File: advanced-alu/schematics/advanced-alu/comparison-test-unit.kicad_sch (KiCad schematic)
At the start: 6 parts

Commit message: updated ALU design
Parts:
- added U?: 74LS245, symbol 74xx:74LS245
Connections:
- net CMPi: now also U?.19 (CE); no longer U?.19 (CE)
- net GND: now also U?.19 (CE), U?.10 (GND)
- net HI_TMP_0: now also U?.2 (A0); no longer U?.2 (P0)
- net HI_TMP_1: now also U?.3 (A1); no longer U?.4 (P1)
- net HI_TMP_2: now also U?.4 (A2); no longer U?.6 (P2)
- net HI_TMP_3: now also U?.5 (A3); no longer U?.8 (P3)
- net HI_TMP_4: now also U?.6 (A4); no longer U?.11 (P4)
- net HI_TMP_5: now also U?.7 (A5); no longer U?.13 (P5)
- net HI_TMP_6: now also U?.8 (A6); no longer U?.15 (P6)
- net HI_TMP_7: now also U?.9 (A7); no longer U?.17 (P7)
- net VCC: now also U?.1 (A->B), U?.20 (VCC)
- net at U?.12 (Q4), U?.14 (B4), U?.15 (I4): no longer RN?.5 (R4)
- net at U?.13 (B5), U?.14 (I5), U?.14 (Q5): no longer RN?.4 (R3)
- net at U?.12 (B6), U?.13 (I6), U?.16 (Q6): no longer RN?.3 (R2)
- net at U?.11 (B7), U?.12 (I7), U?.18 (Q7): no longer RN?.2 (R1)
- net at U?.18 (B0), U?.3 (Q0), U?.4 (I0): no longer RN?.9 (R8)
- net at U?.17 (B1), U?.3 (I1), U?.5 (Q1): no longer RN?.8 (R7)
- net at U?.16 (B2), U?.2 (I2), U?.7 (Q2): no longer RN?.7 (R6)
- net at U?.1 (I3), U?.15 (B3), U?.9 (Q3): no longer RN?.6 (R5)
- new net: RN?.5 (R4), U?.11 (P4), U?.14 (B4)
- new net: RN?.4 (R3), U?.13 (B5), U?.13 (P5)
- new net: RN?.3 (R2), U?.12 (B6), U?.15 (P6)
- new net: RN?.2 (R1), U?.11 (B7), U?.17 (P7)
- new net: RN?.9 (R8), U?.18 (B0), U?.2 (P0)
- new net: RN?.8 (R7), U?.17 (B1), U?.4 (P1)
- new net: RN?.7 (R6), U?.16 (B2), U?.6 (P2)
- new net: RN?.6 (R5), U?.15 (B3), U?.8 (P3)
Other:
- note added: "In CMP mode, the E(quals) flag is set when data bus and HI_TMP values are equal, and the O(verflow) flag is set when value in HI_TMP register is greater than the value on the data bus. Otherwise, E flag is set when data bus value is zero."
- note removed: "In CMP mode, the E(quals) flag is set when values are equal, and the O(verflow) flag is set when value in HI_TMP register is greater than the value on the data bus."
- moved on the sheet: RN?

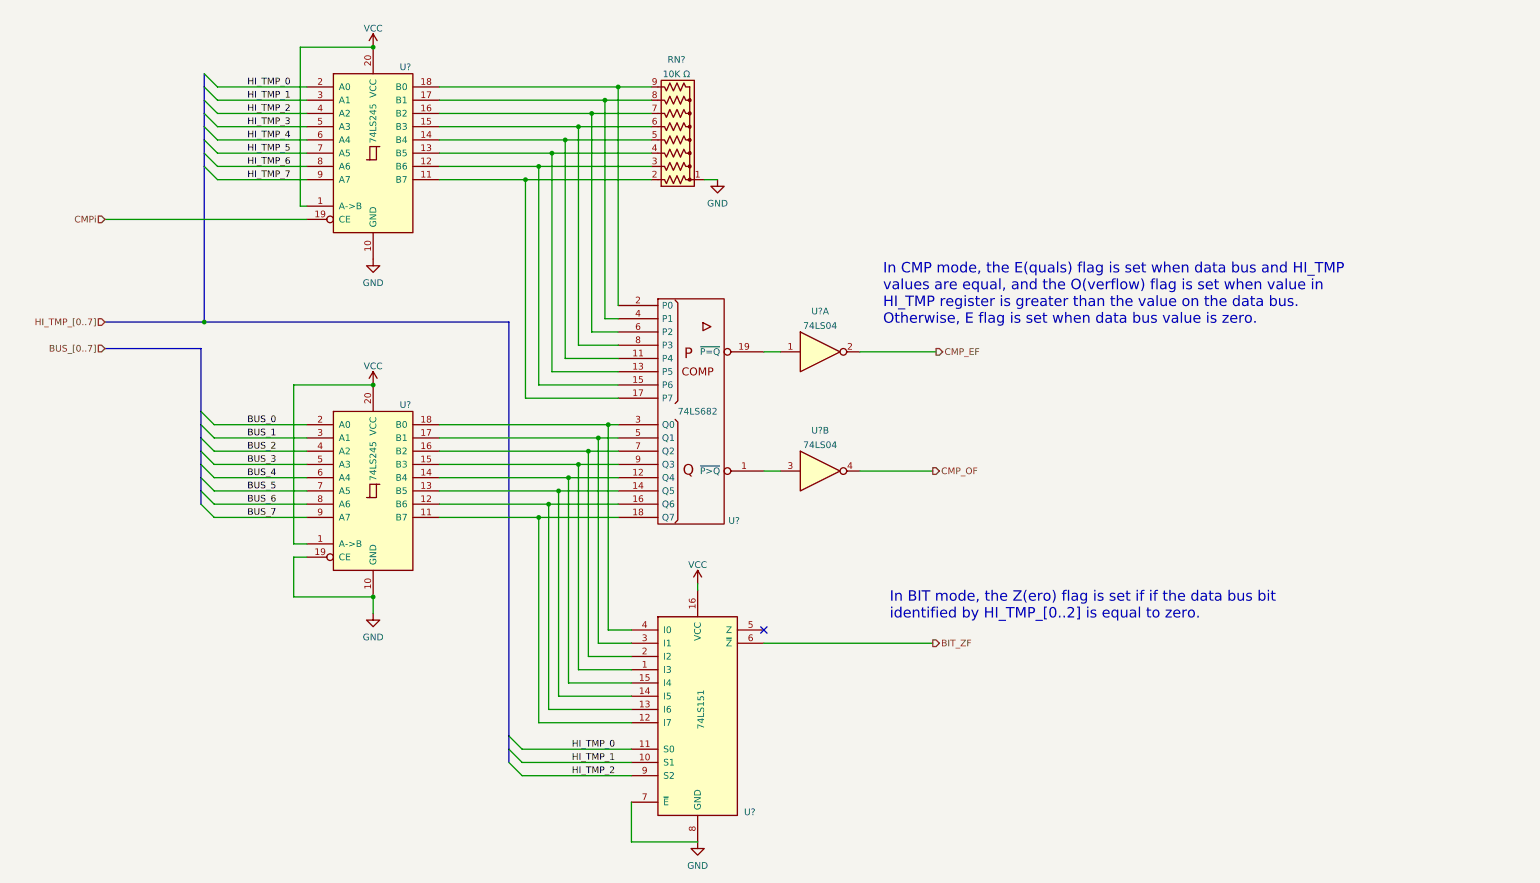
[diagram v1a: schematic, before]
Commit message: updated flags register
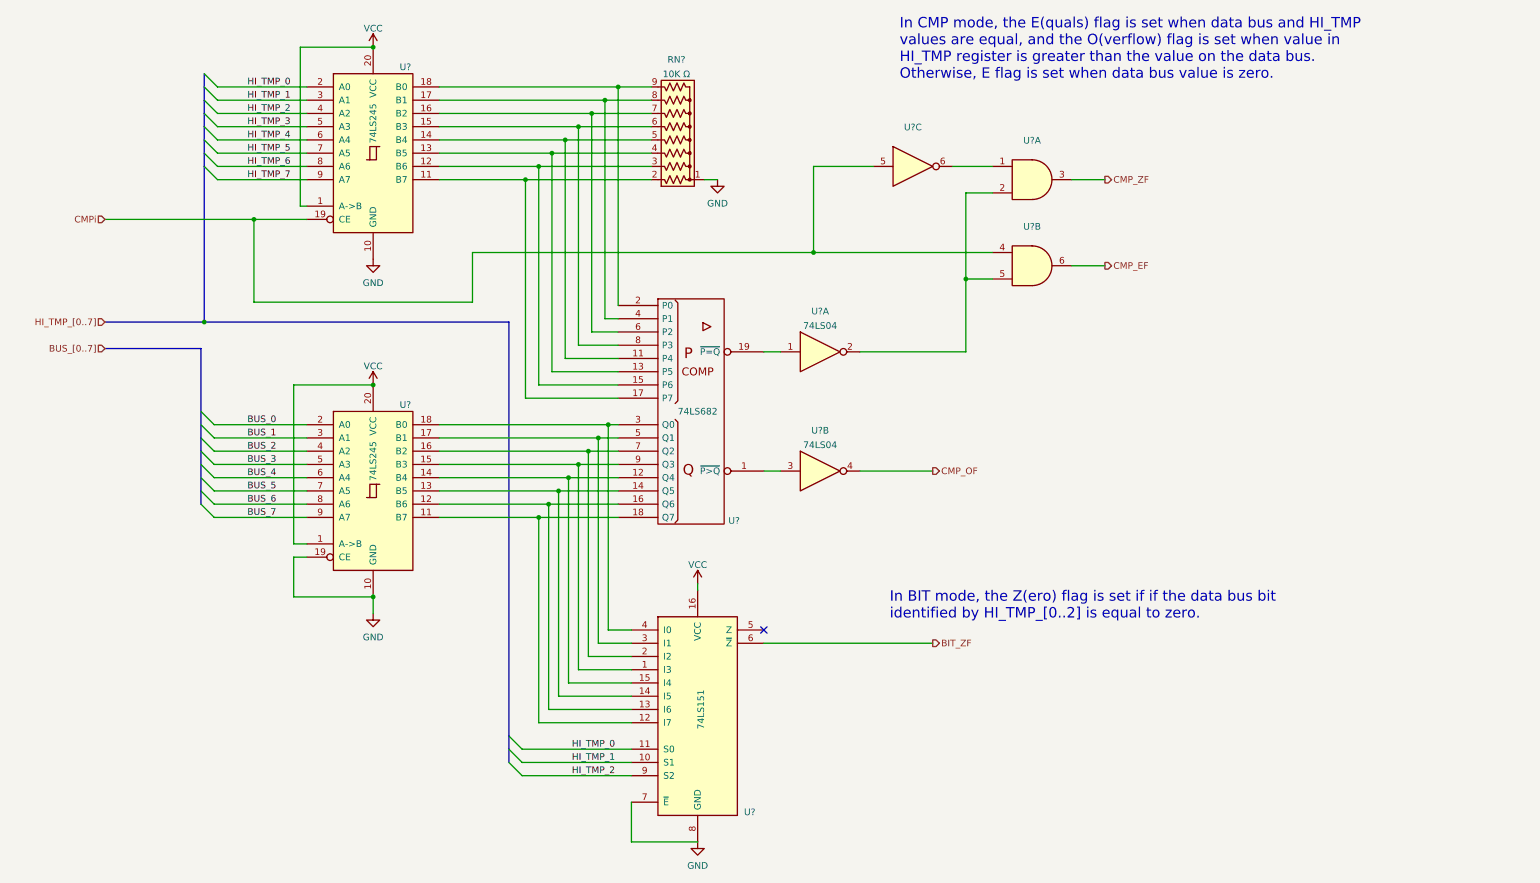
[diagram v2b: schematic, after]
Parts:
- added U? (x2): (no value), symbol 74xx:74LS08
- added U?: (no value), symbol 74xx:74LS04
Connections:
- net CMP_EF: now also U?.6; no longer U?.2
- net CMPi: now also U?.4, U?.5
- new net: U?.1, U?.6
- new net: U?.2, U?.2, U?.5
- new net CMP_ZF: U?.3
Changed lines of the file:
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@@
   (junction (at 114.3 46.99) (diameter 0) (color 0 0 0 0)
   )
+  (junction (at 59.69 57.15) (diameter 0) (color 0 0 0 0)
+  )
   (junction (at 121.92 39.37) (diameter 0) (color 0 0 0 0)
   )
@@
   (junction (at 82.55 129.54) (diameter 0) (color 0 0 0 0)
   )
+  (junction (at 196.215 68.58) (diameter 0) (color 0 0 0 0)
+  )
   (junction (at 82.55 88.9) (diameter 0) (color 0 0 0 0)
   )
@@
   )
   (junction (at 114.3 114.3) (diameter 0) (color 0 0 0 0)
+  )
+  (junction (at 167.005 63.5) (diameter 0) (color 0 0 0 0)
   )
   (junction (at 121.92 104.14) (diameter 0) (color 0 0 0 0)
@@
     (stroke (width 0) (type default) (color 0 0 0 0))
   )
+  (wire (pts (xy 59.69 57.15) (xy 69.85 57.15))
+    (stroke (width 0) (type default) (color 0 0 0 0))
+  )
   (wire (pts (xy 123.825 140.97) (xy 132.08 140.97))
     (stroke (width 0) (type default) (color 0 0 0 0))
@@
     (stroke (width 0) (type default) (color 0 0 0 0))
   )
+  (wire (pts (xy 167.005 63.5) (xy 167.005 46.99))
+    (stroke (width 0) (type default) (color 0 0 0 0))
+  )
   (wire (pts (xy 121.92 143.51) (xy 132.08 143.51))
     (stroke (width 0) (type default) (color 0 0 0 0))
@@
     (stroke (width 0) (type default) (color 0 0 0 0))
   )
+  (wire (pts (xy 101.6 63.5) (xy 167.005 63.5))
+    (stroke (width 0) (type default) (color 0 0 0 0))
+  )
+  (wire (pts (xy 193.675 46.99) (xy 201.295 46.99))
+    (stroke (width 0) (type default) (color 0 0 0 0))
+  )
   (wire (pts (xy 52.705 41.91) (xy 69.85 41.91))
     (stroke (width 0) (type default) (color 0 0 0 0))
@@
     (stroke (width 0) (type default) (color 0 0 0 0))
   )
+  (wire (pts (xy 59.69 57.15) (xy 59.69 73.025))
+    (stroke (width 0) (type default) (color 0 0 0 0))
+  )
   (wire (pts (xy 82.55 129.54) (xy 82.55 132.715))
     (stroke (width 0) (type default) (color 0 0 0 0))
@@
     (stroke (width 0) (type default) (color 0 0 0 0))
   )
+  (wire (pts (xy 101.6 73.025) (xy 101.6 63.5))
+    (stroke (width 0) (type default) (color 0 0 0 0))
+  )
   (wire (pts (xy 144.78 127) (xy 144.78 128.27))
     (stroke (width 0) (type default) (color 0 0 0 0))
@@
     (stroke (width 0) (type default) (color 0 0 0 0))
   )
+  (wire (pts (xy 167.005 46.99) (xy 178.435 46.99))
+    (stroke (width 0) (type default) (color 0 0 0 0))
+  )
   (wire (pts (xy 95.25 114.3) (xy 114.3 114.3))
     (stroke (width 0) (type default) (color 0 0 0 0))
   )
+  (wire (pts (xy 175.895 82.55) (xy 196.215 82.55))
+    (stroke (width 0) (type default) (color 0 0 0 0))
+  )
   (bus (pts (xy 49.53 109.22) (xy 49.53 106.68))
     (stroke (width 0) (type default) (color 0 0 0 0))
   )
+  (wire (pts (xy 201.295 52.07) (xy 196.215 52.07))
+    (stroke (width 0) (type default) (color 0 0 0 0))
+  )
   (wire (pts (xy 52.705 44.45) (xy 69.85 44.45))
     (stroke (width 0) (type default) (color 0 0 0 0))
@@
     (stroke (width 0) (type default) (color 0 0 0 0))
   )
+  (wire (pts (xy 196.215 68.58) (xy 201.295 68.58))
+    (stroke (width 0) (type default) (color 0 0 0 0))
+  )
   (wire (pts (xy 123.825 101.6) (xy 129.54 101.6))
     (stroke (width 0) (type default) (color 0 0 0 0))
@@
     (stroke (width 0) (type default) (color 0 0 0 0))
   )
+  (wire (pts (xy 196.215 52.07) (xy 196.215 68.58))
+    (stroke (width 0) (type default) (color 0 0 0 0))
+  )
   (wire (pts (xy 68.58 54.61) (xy 68.58 24.13))
     (stroke (width 0) (type default) (color 0 0 0 0))
@@
     (stroke (width 0) (type default) (color 0 0 0 0))
   )
+  (wire (pts (xy 216.535 49.53) (xy 222.885 49.53))
+    (stroke (width 0) (type default) (color 0 0 0 0))
+  )
   (wire (pts (xy 52.705 39.37) (xy 69.85 39.37))
     (stroke (width 0) (type default) (color 0 0 0 0))
@@
     (stroke (width 0) (type default) (color 0 0 0 0))
   )
-  (wire (pts (xy 31.115 57.15) (xy 69.85 57.15))
+  (wire (pts (xy 31.115 57.15) (xy 59.69 57.15))
     (stroke (width 0) (type default) (color 0 0 0 0))
   )
@@
     (stroke (width 0) (type default) (color 0 0 0 0))
   )
+  (wire (pts (xy 167.005 63.5) (xy 201.295 63.5))
+    (stroke (width 0) (type default) (color 0 0 0 0))
+  )
   (wire (pts (xy 52.705 31.75) (xy 69.85 31.75))
     (stroke (width 0) (type default) (color 0 0 0 0))
   )
+  (wire (pts (xy 216.535 66.04) (xy 222.885 66.04))
+    (stroke (width 0) (type default) (color 0 0 0 0))
+  )
   (wire (pts (xy 52.07 99.06) (xy 69.85 99.06))
     (stroke (width 0) (type default) (color 0 0 0 0))
@@
     (stroke (width 0) (type default) (color 0 0 0 0))
   )
+  (wire (pts (xy 59.69 73.025) (xy 101.6 73.025))
+    (stroke (width 0) (type default) (color 0 0 0 0))
+  )
   (wire (pts (xy 121.92 81.28) (xy 129.54 81.28))
     (stroke (width 0) (type default) (color 0 0 0 0))
@@
     (stroke (width 0) (type default) (color 0 0 0 0))
   )
-  (wire (pts (xy 175.895 82.55) (xy 190.5 82.55))
+  (wire (pts (xy 196.215 68.58) (xy 196.215 82.55))
     (stroke (width 0) (type default) (color 0 0 0 0))
   )
@@
   )
   (text "In CMP mode, the E(quals) flag is set when data bus and HI_TMP\nvalues are equal, and the O(verflow) flag is set when value in\nHI_TMP register is greater than the value on the data bus.\nOtherwise, E flag is set when data bus value is zero."
-    (at 180.34 77.47 0)
+    (at 183.515 30.48 0)
     (effects (font (size 2 2)) (justify left bottom))
   )
@@
     (effects (font (size 1.27 1.27)) (justify right))
   )
-  (hierarchical_label "CMP_EF" (shape output) (at 190.5 82.55 0)
+  (hierarchical_label "CMP_EF" (shape output) (at 222.885 66.04 0)
+    (effects (font (size 1.27 1.27)) (justify left))
+  )
+  (hierarchical_label "CMP_ZF" (shape output) (at 222.885 49.53 0)
     (effects (font (size 1.27 1.27)) (justify left))
   )
@@
     (pin "8")
     (pin "9")
+  )
+  (symbol (lib_id "74xx:74LS08") (at 208.915 49.53 0) (unit 1)
+    (in_bom yes) (on_board yes) (fields_autoplaced)
+    (property "Reference" "U?" (id 0) (at 208.915 42.0202 0))
+    (property "Value" "" (id 1) (at 208.915 44.5571 0))
+    (property "Footprint" "" (id 2) (at 208.915 49.53 0)
+      (effects (font (size 1.27 1.27)) hide)
+    )
+    (property "Datasheet" "http://www.ti.com/lit/gpn/sn74LS08" (id 3) (at 208.915 49.53 0)
+      (effects (font (size 1.27 1.27)) hide)
+    )
+    (pin "1")
+    (pin "2")
+    (pin "3")
+    (pin "4")
+    (pin "5")
+    (pin "6")
+    (pin "10")
+    (pin "8")
+    (pin "9")
+    (pin "11")
+    (pin "12")
+    (pin "13")
+    (pin "14")
+    (pin "7")
   )
   (symbol (lib_id "power:GND") (at 148.59 49.53 0) (unit 1)
@@
     (pin "9")
   )
+  (symbol (lib_id "74xx:74LS08") (at 208.915 66.04 0) (unit 2)
+    (in_bom yes) (on_board yes) (fields_autoplaced)
+    (property "Reference" "U?" (id 0) (at 208.915 58.5302 0))
+    (property "Value" "" (id 1) (at 208.915 61.0671 0))
+    (property "Footprint" "" (id 2) (at 208.915 66.04 0)
+      (effects (font (size 1.27 1.27)) hide)
+    )
+    (property "Datasheet" "http://www.ti.com/lit/gpn/sn74LS08" (id 3) (at 208.915 66.04 0)
+      (effects (font (size 1.27 1.27)) hide)
+    )
+    (pin "1")
+    (pin "2")
+    (pin "3")
+    (pin "4")
+    (pin "5")
+    (pin "6")
+    (pin "10")
+    (pin "8")
+    (pin "9")
+    (pin "11")
+    (pin "12")
+    (pin "13")
+    (pin "14")
+    (pin "7")
+  )
   (symbol (lib_id "74xx:74LS245") (at 82.55 109.22 0) (unit 1)
     (in_bom yes) (on_board yes)
@@
     (pin "9")
   )
+  (symbol (lib_id "74xx:74LS04") (at 186.055 46.99 0) (unit 3)
+    (in_bom yes) (on_board yes) (fields_autoplaced)
+    (property "Reference" "U?" (id 0) (at 186.055 39.4802 0))
+    (property "Value" "" (id 1) (at 186.055 42.0171 0))
+    (property "Footprint" "" (id 2) (at 186.055 46.99 0)
+      (effects (font (size 1.27 1.27)) hide)
+    )
+    (property "Datasheet" "http://www.ti.com/lit/gpn/sn74LS04" (id 3) (at 186.055 46.99 0)
+      (effects (font (size 1.27 1.27)) hide)
+    )
+    (pin "1")
+    (pin "2")
+    (pin "3")
+    (pin "4")
+    (pin "5")
+    (pin "6")
+    (pin "8")
+    (pin "9")
+    (pin "10")
+    (pin "11")
+    (pin "12")
+    (pin "13")
+    (pin "14")
+    (pin "7")
+  )
   (symbol (lib_id "power:VCC") (at 82.55 88.9 0) (unit 1)

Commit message: updated I and J registers and step counter logic
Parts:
- U? (x2): value (none) -> 74LS08
- U?: value (none) -> 74LS04
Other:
- note added: "In CMP mode, the E(quals) flag is set when data bus and HI_TMP values are equal, and the O(verflow) flag is set when value in HI_TMP register is greater than the value on the data bus. Otherwise, Z(ero) flag is set when data bus value is zero."
- note removed: "In CMP mode, the E(quals) flag is set when data bus and HI_TMP values are equal, and the O(verflow) flag is set when value in HI_TMP register is greater than the value on the data bus. Otherwise, E flag is set when data bus value is zero."
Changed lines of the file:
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@@
     (effects (font (size 2 2)) (justify left bottom))
   )
-  (text "In CMP mode, the E(quals) flag is set when data bus and HI_TMP\nvalues are equal, and the O(verflow) flag is set when value in\nHI_TMP register is greater than the value on the data bus.\nOtherwise, E flag is set when data bus value is zero."
+  (text "In CMP mode, the E(quals) flag is set when data bus and HI_TMP\nvalues are equal, and the O(verflow) flag is set when value in\nHI_TMP register is greater than the value on the data bus.\nOtherwise, Z(ero) flag is set when data bus value is zero."
     (at 183.515 30.48 0)
     (effects (font (size 2 2)) (justify left bottom))
@@
     (in_bom yes) (on_board yes) (fields_autoplaced)
     (property "Reference" "U?" (id 0) (at 208.915 42.0202 0))
-    (property "Value" "" (id 1) (at 208.915 44.5571 0))
+    (property "Value" "74LS08" (id 1) (at 208.915 44.5571 0))
     (property "Footprint" "" (id 2) (at 208.915 49.53 0)
       (effects (font (size 1.27 1.27)) hide)
@@
     (in_bom yes) (on_board yes) (fields_autoplaced)
     (property "Reference" "U?" (id 0) (at 208.915 58.5302 0))
-    (property "Value" "" (id 1) (at 208.915 61.0671 0))
+    (property "Value" "74LS08" (id 1) (at 208.915 61.0671 0))
     (property "Footprint" "" (id 2) (at 208.915 66.04 0)
       (effects (font (size 1.27 1.27)) hide)
@@
     (in_bom yes) (on_board yes) (fields_autoplaced)
     (property "Reference" "U?" (id 0) (at 186.055 39.4802 0))
-    (property "Value" "" (id 1) (at 186.055 42.0171 0))
+    (property "Value" "74LS04" (id 1) (at 186.055 42.0171 0))
     (property "Footprint" "" (id 2) (at 186.055 46.99 0)
       (effects (font (size 1.27 1.27)) hide)

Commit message: updated documentation
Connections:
- net CMPi renamed CMPs
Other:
- note added: "When CPMs is HIGH, the E(quals) flag is set when data bus and HI_TMP values are equal, and the O(verflow) flag is set when value in HI_TMP register is greater than the value on the data bus. Otherwise, Z(ero) flag is set when data bus value is zero."
- note removed: "In CMP mode, the E(quals) flag is set when data bus and HI_TMP values are equal, and the O(verflow) flag is set when value in HI_TMP register is greater than the value on the data bus. Otherwise, Z(ero) flag is set when data bus value is zero."
- title: (none) -> Advanced Arithmetic Logic Unit - Comparison Unit
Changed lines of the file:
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@@
 (kicad_sch (version 20211123) (generator eeschema)
   (paper "A4")
+  (title_block
+    (title "Advanced Arithmetic Logic Unit - Comparison Unit")
+  )
   (junction (at 119.38 41.91) (diameter 0) (color 0 0 0 0)
   )
@@
     (effects (font (size 2 2)) (justify left bottom))
   )
-  (text "In CMP mode, the E(quals) flag is set when data bus and HI_TMP\nvalues are equal, and the O(verflow) flag is set when value in\nHI_TMP register is greater than the value on the data bus.\nOtherwise, Z(ero) flag is set when data bus value is zero."
-    (at 183.515 30.48 0)
+  (text "When CPMs is HIGH, the E(quals) flag is set when data bus and HI_TMP\nvalues are equal, and the O(verflow) flag is set when value in\nHI_TMP register is greater than the value on the data bus.\nOtherwise, Z(ero) flag is set when data bus value is zero."
+    (at 170.942 30.226 0)
     (effects (font (size 2 2)) (justify left bottom))
   )
@@
     (effects (font (size 1.27 1.27)) (justify right))
   )
-  (hierarchical_label "CMPi" (shape input) (at 31.115 57.15 180)
+  (hierarchical_label "CMPs" (shape input) (at 31.115 57.15 180)
     (effects (font (size 1.27 1.27)) (justify right))
   )
